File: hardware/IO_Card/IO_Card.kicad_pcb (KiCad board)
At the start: 2 copper layers, 100 x 99.9 mm, 6 parts, among them J1 6502 Edge, J2 6502 Pinheader, U1 W65C22NxP

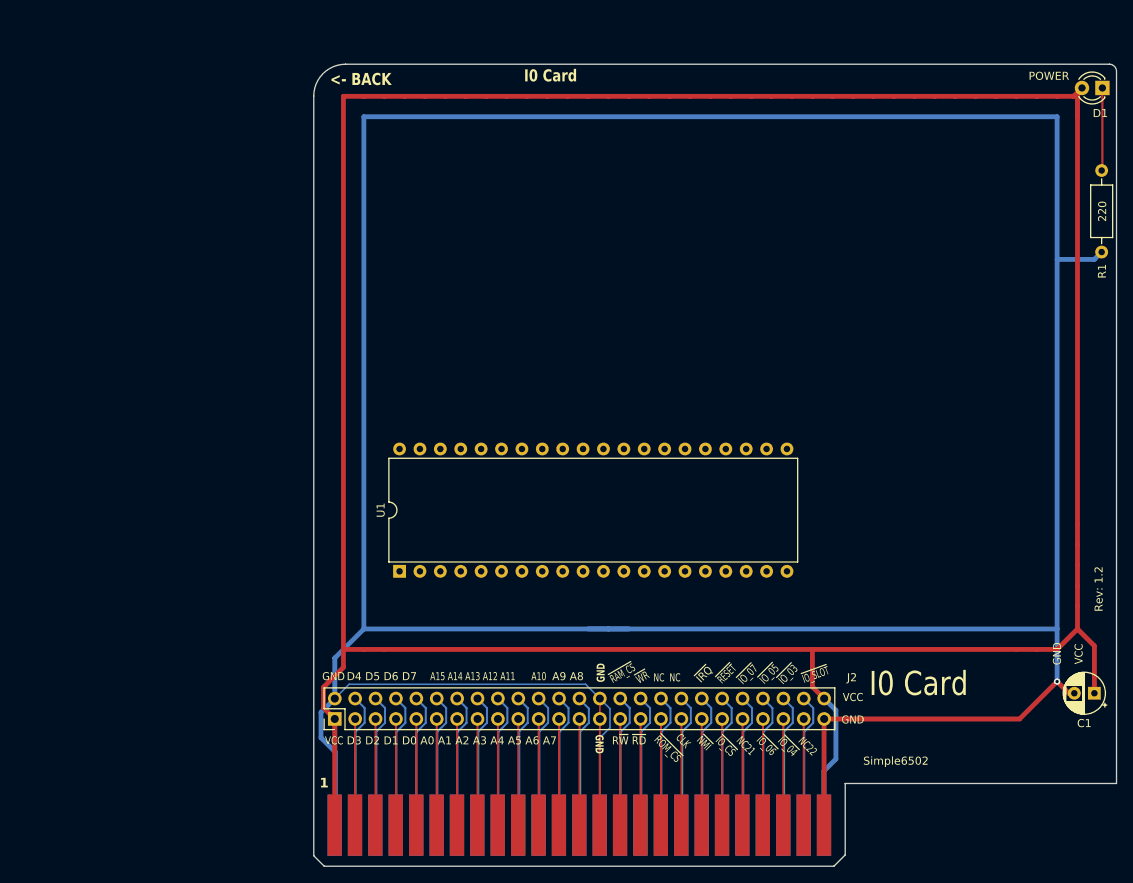
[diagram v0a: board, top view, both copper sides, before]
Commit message: flipped card PCB to face the correct way
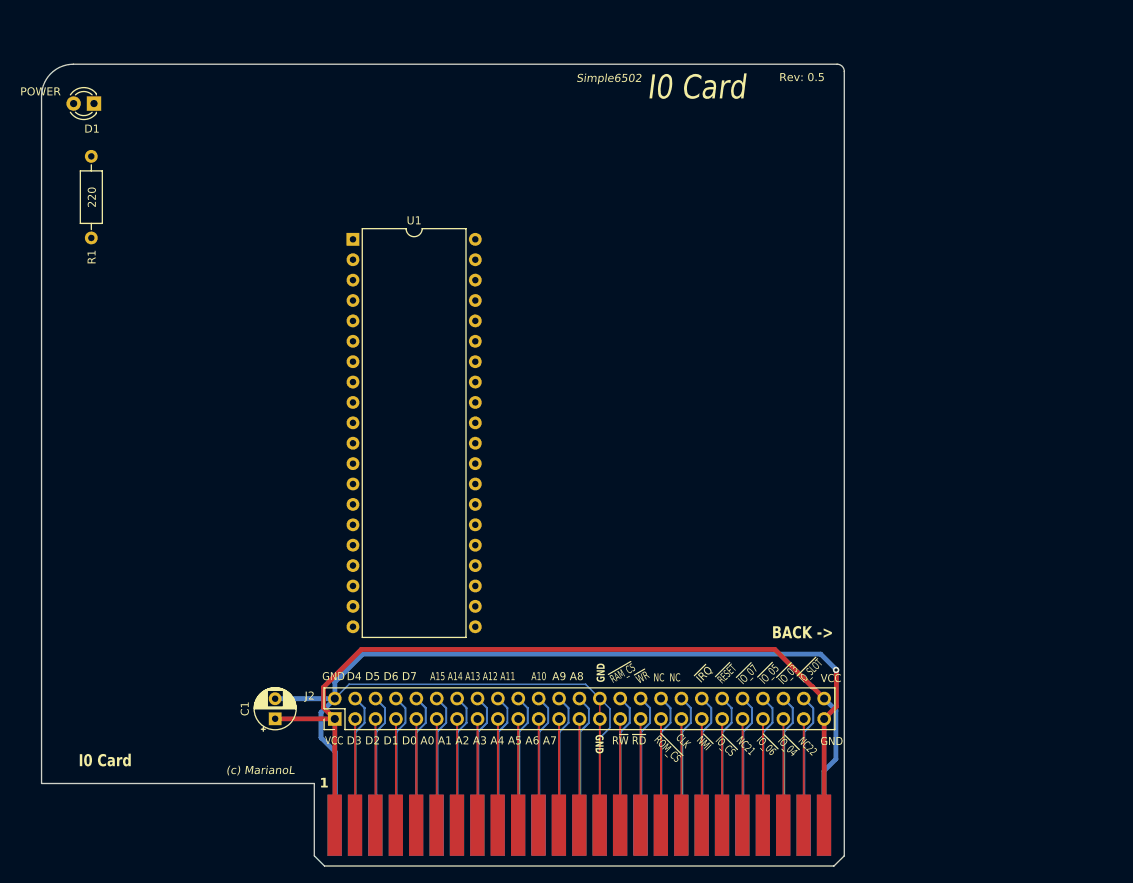
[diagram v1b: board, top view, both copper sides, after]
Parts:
- moved R1 125.9 mm to (26.0, 42.1)
- moved D1 125.6 mm to (26.3, 35.5)
- moved C1 102.1 mm to (48.9, 112.1), turned to 90 degrees
- moved U1 41.8 mm to (58.6, 52.4), turned to 0 degrees
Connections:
- U1 pad 22: unconnected-(U1-R/~{W}-Pad22) -> /R~{W}
- U1 pad 25: unconnected-(U1-ϕ2-Pad25) -> /CLK
- U1 pad 26: unconnected-(U1-D7-Pad26) -> /D7
- U1 pad 27: unconnected-(U1-D6-Pad27) -> /D6
- U1 pad 28: unconnected-(U1-D5-Pad28) -> /D5
- U1 pad 29: unconnected-(U1-D4-Pad29) -> /D4
- U1 pad 30: unconnected-(U1-D3-Pad30) -> /D3
- U1 pad 31: unconnected-(U1-D2-Pad31) -> /D2
- U1 pad 32: unconnected-(U1-D1-Pad32) -> /D1
- U1 pad 33: unconnected-(U1-D0-Pad33) -> /D0
- U1 pad 34: unconnected-(U1-~{RES}-Pad34) -> /~{RESET}
- U1 pad 35: unconnected-(U1-RS3-Pad35) -> /A3
- U1 pad 36: unconnected-(U1-RS2-Pad36) -> /A2
- U1 pad 37: unconnected-(U1-RS1-Pad37) -> /A1
- U1 pad 38: unconnected-(U1-RS0-Pad38) -> /A0
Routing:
- net GND: track 459.4 -> 178.6 mm
- net VCC: track 380.1 -> 109.1 mm
- net Net-(D1-K): track 10.3 -> 0.00 mm
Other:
- outline, holes or cut-outs redrawn
- board text added: "(c) MarianoL"
- board text added: "BACK ->"
- board text removed: "<- BACK"

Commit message: Rev: 0.5 basic VIA wiring
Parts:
- added D2: 1N6263, Diode_THT:D_DO-35_SOD27_P7.62mm_Horizontal, F.Cu at (85.1, 100.8)
- added J3: Port A, Connector_PinHeader_2.54mm:PinHeader_2x07_P2.54mm_Horizontal, F.Cu at (113.2, 55.0)
- added J4: Port B, Connector_PinHeader_2.54mm:PinHeader_2x07_P2.54mm_Horizontal, F.Cu at (113.2, 80.0)
- added J5: IO Select, Connector_PinHeader_2.54mm:PinHeader_2x04_P2.54mm_Vertical, F.Cu at (108.3, 96.9)
- moved R1 8.85 mm to (31.8, 35.4), turned to 0 degrees
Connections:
- net /~{IRQ} renamed ~{IRQ}
- U1 pad 10: unconnected-(U1-PB0-Pad10) -> /PB0
- U1 pad 11: unconnected-(U1-PB1-Pad11) -> /PB1
- U1 pad 12: unconnected-(U1-PB2-Pad12) -> /PB2
- U1 pad 13: unconnected-(U1-PB3-Pad13) -> /PB3
- U1 pad 14: unconnected-(U1-PB4-Pad14) -> /PB4
- U1 pad 15: unconnected-(U1-PB5-Pad15) -> /PB5
- U1 pad 16: unconnected-(U1-PB6-Pad16) -> /PB6
- U1 pad 17: unconnected-(U1-PB7-Pad17) -> /PB7
- U1 pad 18: unconnected-(U1-CB1-Pad18) -> /CB1
- U1 pad 19: unconnected-(U1-CB2-Pad19) -> /CB2
- U1 pad 2: unconnected-(U1-PA0-Pad2) -> /PA0
- U1 pad 21: unconnected-(U1-~{IRQ}-Pad21) -> ~{IRQ_V1}
- U1 pad 23: unconnected-(U1-~{CS2}-Pad23) -> ~{CS_V1}
- U1 pad 3: unconnected-(U1-PA1-Pad3) -> /PA1
- U1 pad 39: unconnected-(U1-CA2-Pad39) -> /CA2
- U1 pad 4: unconnected-(U1-PA2-Pad4) -> /PA2
- U1 pad 40: unconnected-(U1-CA1-Pad40) -> /CA1
- U1 pad 5: unconnected-(U1-PA3-Pad5) -> /PA3
- U1 pad 6: unconnected-(U1-PA4-Pad6) -> /PA4
- U1 pad 7: unconnected-(U1-PA5-Pad7) -> /PA5
- U1 pad 8: unconnected-(U1-PA6-Pad8) -> /PA6
- U1 pad 9: unconnected-(U1-PA7-Pad9) -> /PA7
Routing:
- net GND: track 178.6 -> 60.1 mm, vias 1 -> 2
- net VCC: track 109.1 -> 177.4 mm
- added copper zone on B.Cu, net GND

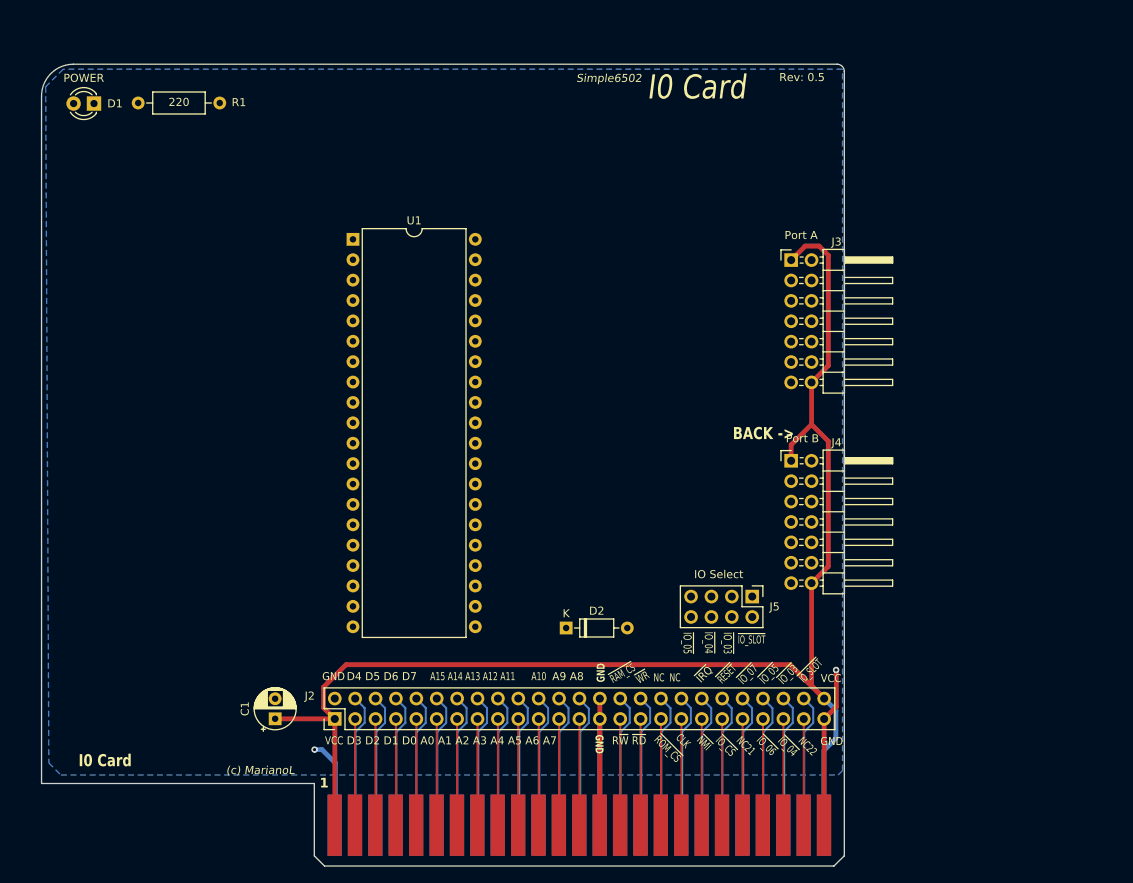
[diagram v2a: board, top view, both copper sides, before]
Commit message: Rev 0.6 2 VIAs ready to route
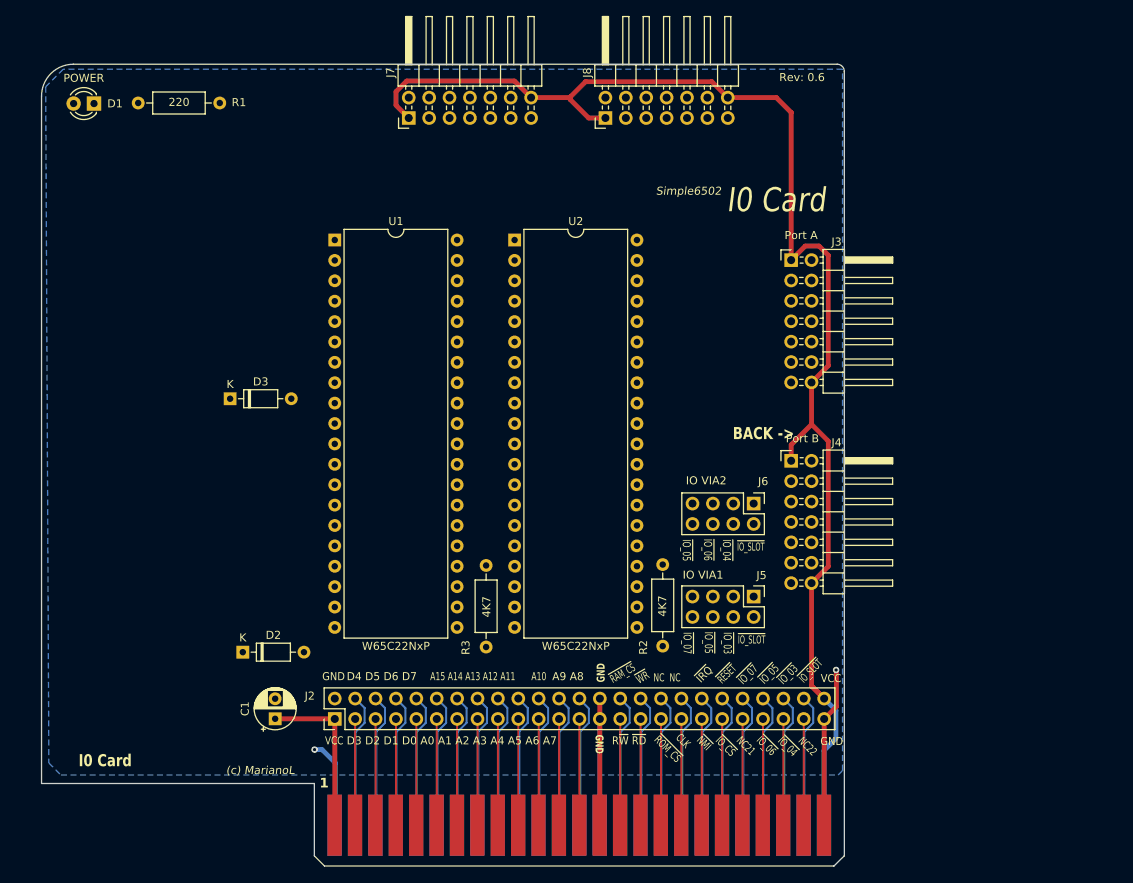
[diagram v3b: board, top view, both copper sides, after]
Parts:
- added D3: 1N6263, Diode_THT:D_DO-35_SOD27_P7.62mm_Horizontal, F.Cu at (43.3, 72.3)
- added J6: IO VIA2, Connector_PinHeader_2.54mm:PinHeader_2x04_P2.54mm_Vertical, F.Cu at (108.5, 85.3)
- added J7: Port A, Connector_PinHeader_2.54mm:PinHeader_2x07_P2.54mm_Horizontal, F.Cu at (65.5, 37.3)
- added J8: Port B, Connector_PinHeader_2.54mm:PinHeader_2x07_P2.54mm_Horizontal, F.Cu at (90.0, 37.3)
- added R2: 4K7, Resistor_THT:R_Axial_DIN0207_L6.3mm_D2.5mm_P10.16mm_Horizontal, F.Cu at (97.2, 92.9)
- added R3: 4K7, Resistor_THT:R_Axial_DIN0207_L6.3mm_D2.5mm_P10.16mm_Horizontal, F.Cu at (75.2, 93.0)
- added U2: W65C22NxP, Package_DIP:DIP-40_W15.24mm, F.Cu at (78.7, 52.5)
- J5: value IO Select -> IO VIA1
- moved D2 40.4 mm to (44.9, 103.8)
- moved U1 2.27 mm to (56.3, 52.5)
- moved J5 0.18 mm to (108.5, 96.9)
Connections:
- J4 pad 3: /PA0 -> /PB0
- J4 pad 5: /PA2 -> /PB2
- J4 pad 7: /PA4 -> /PB4
- J4 pad 9: /PA6 -> /PB6
- J5 pad 6: /~{IO_04} -> /~{IO_05}
- J5 pad 8: /~{IO_05} -> /~{IO_07}
- U1 pad 24: unconnected-(U1-CS1-Pad24) -> Net-(U1-CS1)
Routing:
- net VCC: track 177.4 -> 190.7 mm

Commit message: Routing PCB
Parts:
- removed J5: IO VIA1, Connector_PinHeader_2.54mm:PinHeader_2x04_P2.54mm_Vertical
- removed J6: IO VIA2, Connector_PinHeader_2.54mm:PinHeader_2x04_P2.54mm_Vertical
- added C1: .1uF, Capacitor_THT:C_Disc_D4.3mm_W1.9mm_P5.00mm, F.Cu at (84.7, 100.8)
- added C2: .1uF, Capacitor_THT:C_Disc_D4.3mm_W1.9mm_P5.00mm, F.Cu at (51.7, 97.3)
- added J9: VIA IO Select, Connector_PinHeader_2.54mm:PinHeader_3x06_P2.54mm_Vertical, F.Cu at (116.1, 95.9)
- moved D1 88.6 mm to (114.9, 39.8), turned to 0 degrees
- moved R1 77.4 mm to (108.4, 46.9), turned to 180 degrees
- moved D2 47.5 mm to (92.4, 103.4)
- moved D3 40.4 mm to (69.1, 103.4), turned to 180 degrees
- moved R2 27.0 mm to (71.4, 100.8), turned to 0 degrees
- moved U2 23.0 mm to (56.0, 49.0)
- moved R3 22.1 mm to (97.0, 89.7)
- moved U1 22.0 mm to (78.0, 49.0)
- moved J4 8.39 mm to (113.0, 71.6)
- moved J3 7.24 mm to (113.1, 47.8)
- renumbered C1 to C3
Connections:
- J4 pad 11: /CA1 -> /CB1
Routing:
- net /A0: track 13.2 -> 95.9 mm, vias 0 -> 1
- net VCC: track 190.7 -> 272.1 mm
- net /A1: track 13.2 -> 92.5 mm, vias 0 -> 1
- net /A2: track 13.2 -> 90.2 mm, vias 0 -> 1
- net /A3: track 13.2 -> 88.2 mm, vias 0 -> 1
- net /D0: track 13.2 -> 85.4 mm, vias 0 -> 1
- net /D1: track 13.2 -> 84.4 mm, vias 0 -> 1
- net /D2: track 13.2 -> 84.1 mm, vias 0 -> 1
- net /D3: track 13.2 -> 83.3 mm, vias 0 -> 1
- net /D4: track 16.8 -> 82.5 mm, vias 0 -> 1
- net /D5: track 16.8 -> 78.0 mm, vias 0 -> 1
- net ~{IRQ}: track 16.8 -> 74.6 mm, vias 0 -> 1
- net /D6: track 16.8 -> 73.6 mm, vias 0 -> 1
- net ~{CS_V2}: track 0.00 -> 53.3 mm, vias 0 -> 1
- net /CLK: track 13.2 -> 65.8 mm, vias 0 -> 1
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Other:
- board text added: "VIA 1"
- board text added: "VIA 2"

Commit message: IO Card is Rev 1.0 PCB complete
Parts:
- J3, J4, J7, J8: footprint Connector_PinHeader_2.54mm:PinHeader_2x07_P2.54mm_Horizontal -> Connector_PinHeader_2.54mm:PinHeader_2x07_P2.54mm_Horizontal_Edge
- moved D1 59.4 mm to (55.5, 37.3)
- moved R1 57.4 mm to (51.1, 43.4), turned to -90 degrees
- moved C1 6.63 mm to (78.1, 100.8)
- moved C3 2.67 mm to (50.7, 110.2)
- moved D2 2.51 mm to (89.9, 103.9), turned to 180 degrees
- moved D3 2.23 mm to (71.2, 103.9), turned to 0 degrees
- moved R2 1.87 mm to (69.5, 101.0), turned to 180 degrees
- moved C2 0.94 mm to (52.6, 97.2), turned to -90 degrees
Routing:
- net /2CB2: track 0.00 -> 94.9 mm
- net /2CB1: track 0.00 -> 88.2 mm
- net /2PB7: track 0.00 -> 87.9 mm
- net /~{RESET}: track 39.7 -> 121.1 mm, vias 0 -> 5
- net /2PB6: track 0.00 -> 81.2 mm
- net /2PB5: track 0.00 -> 81.0 mm
- net /2PB4: track 0.00 -> 74.3 mm
- net /2PB3: track 0.00 -> 74.2 mm
- net /2PB2: track 0.00 -> 67.3 mm
- net /2PB1: track 0.00 -> 67.0 mm
- net /2PB0: track 0.00 -> 60.3 mm
- net /2PA7: track 0.00 -> 45.7 mm
- net VCC: track 272.1 -> 317.2 mm, vias 0 -> 3
- net /2PA6: track 0.00 -> 39.1 mm
- net /2PA5: track 0.00 -> 38.8 mm
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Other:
- board size 100 x 99.9 mm -> 79.5 x 99.9 mm

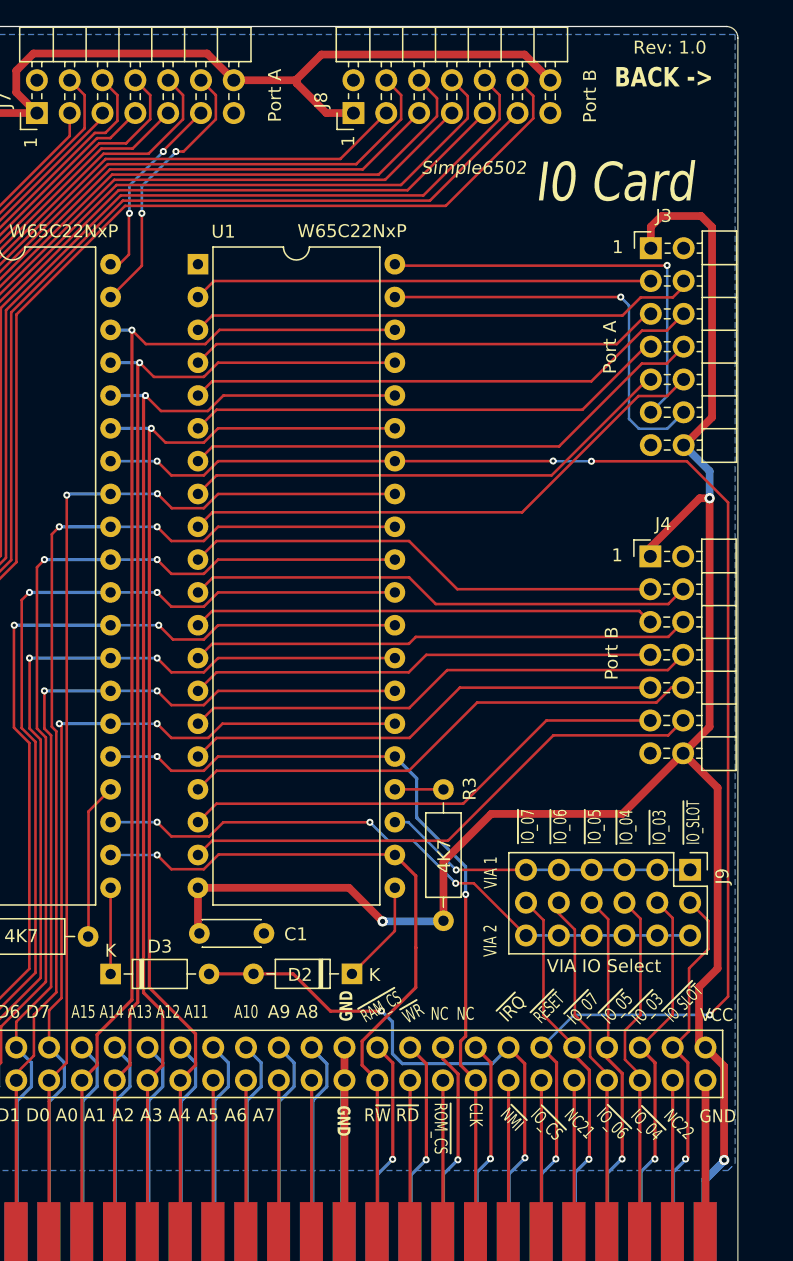
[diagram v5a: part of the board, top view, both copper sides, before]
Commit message: Updates some labels
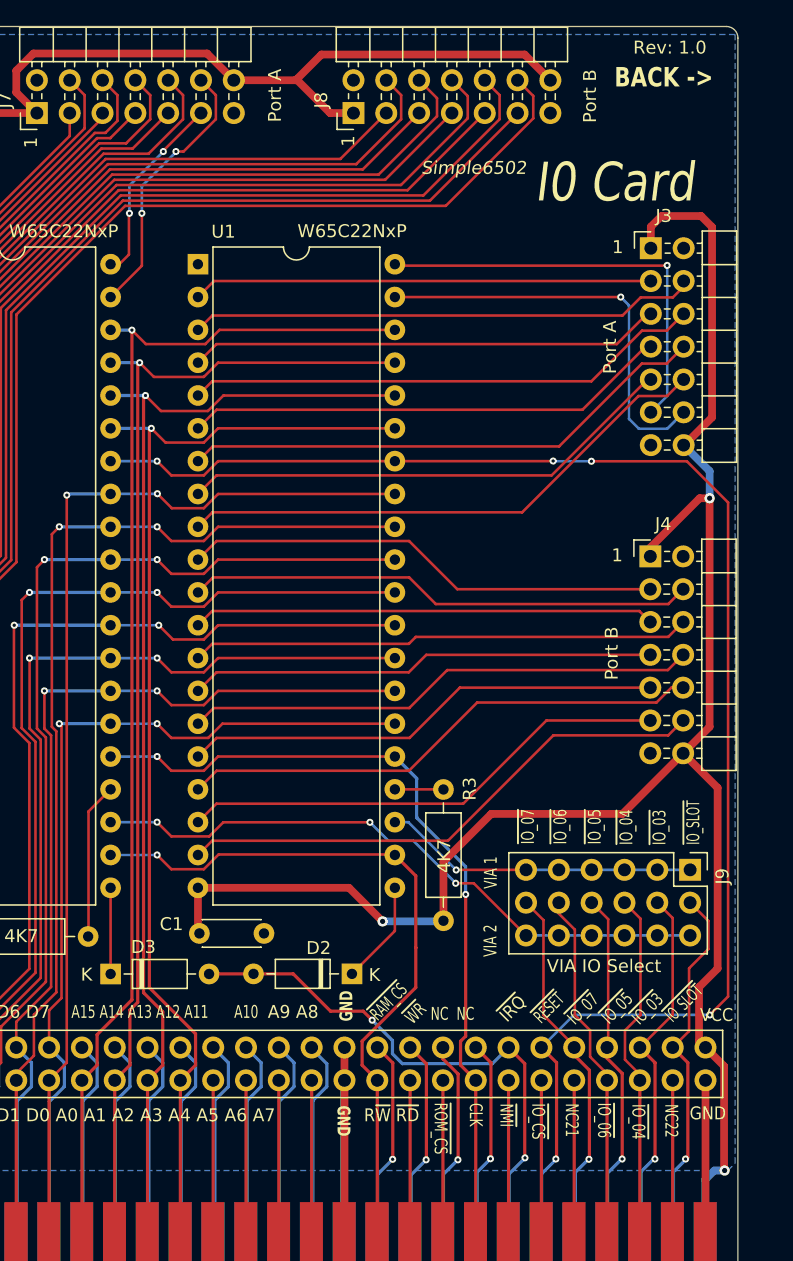
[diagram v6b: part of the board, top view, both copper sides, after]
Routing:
- net ~{IRQ}: track 44.9 -> 44.0 mm
